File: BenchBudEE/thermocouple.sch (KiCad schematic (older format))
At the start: 0 parts

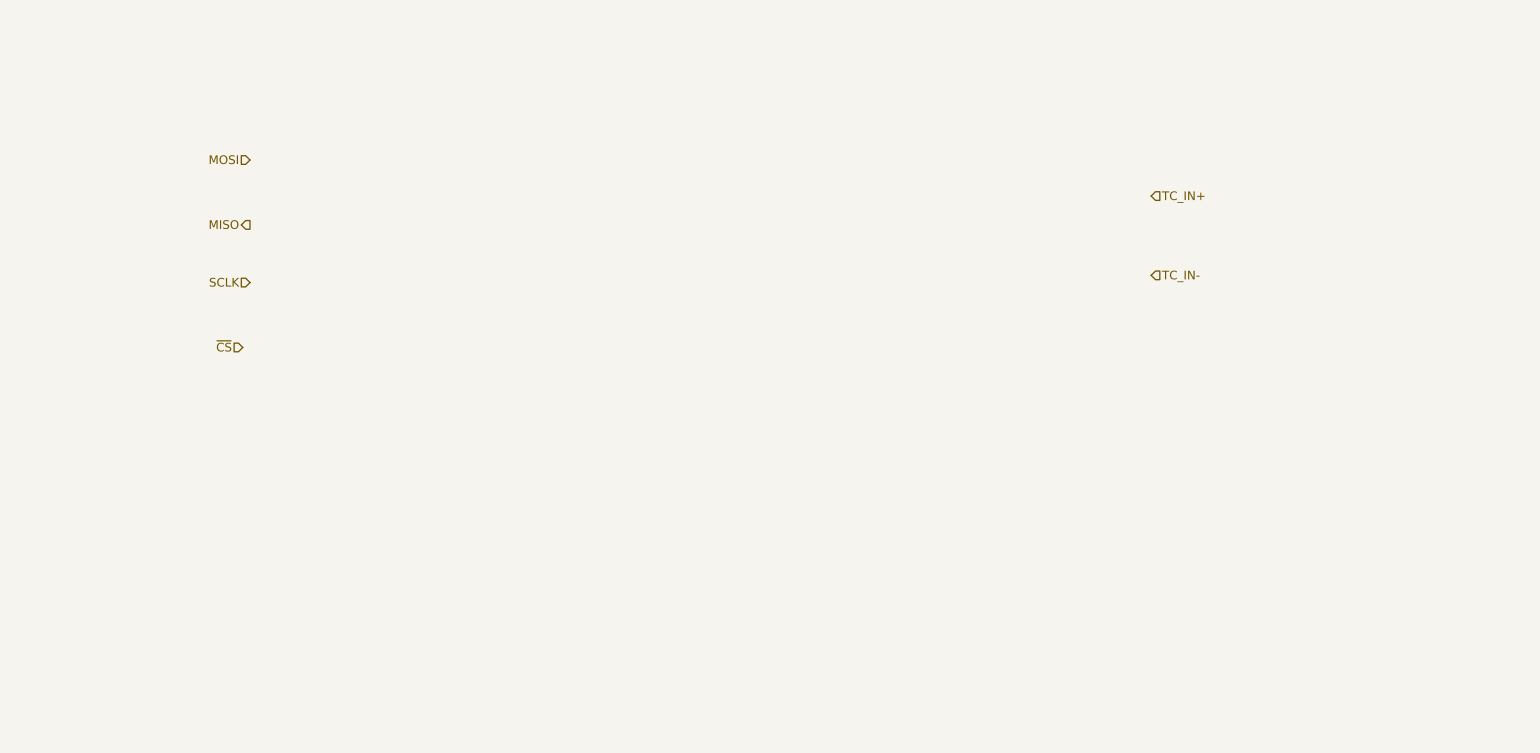
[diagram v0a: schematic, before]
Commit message: blocked TC sheet
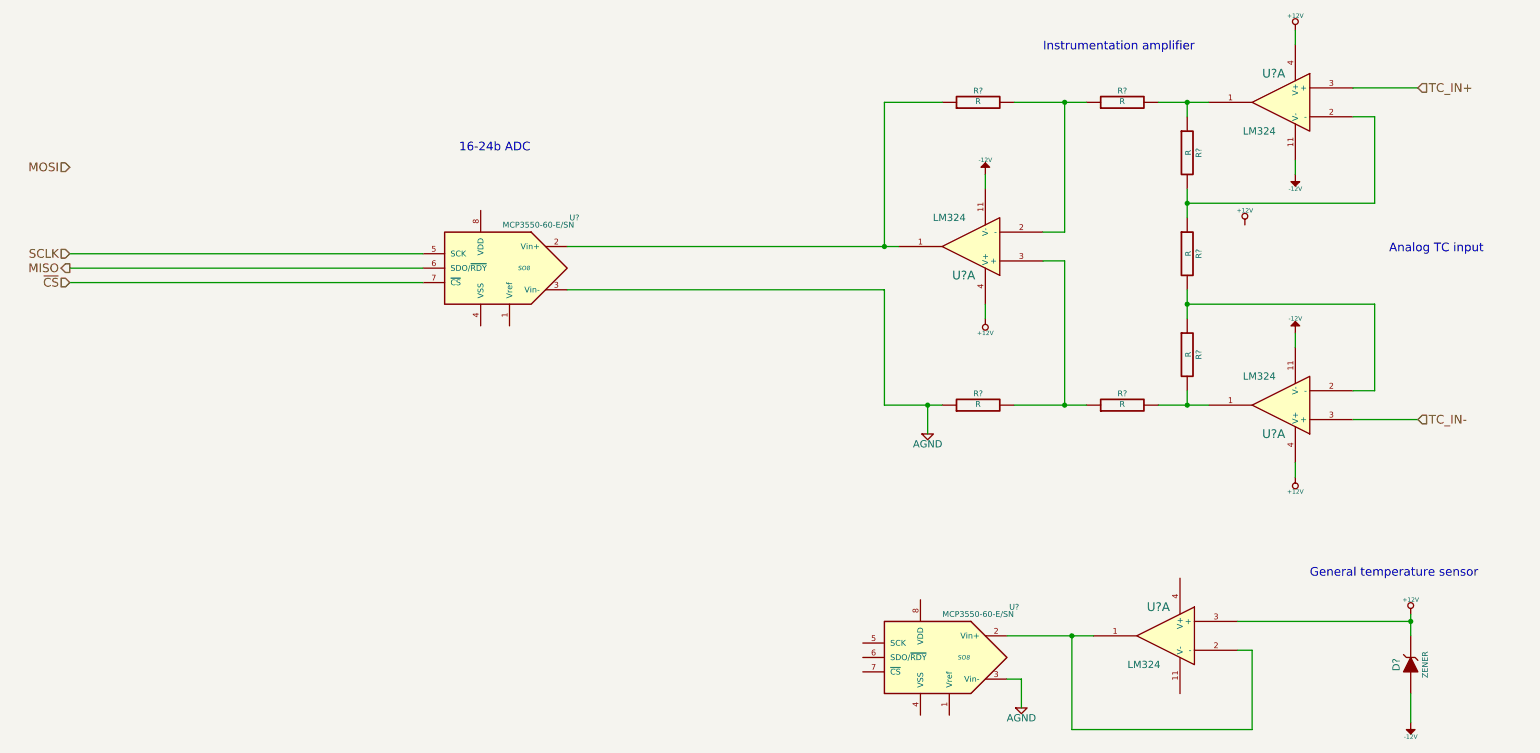
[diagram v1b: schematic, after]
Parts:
- added D?: ZENER, ~, symbol ZENER
- added R? (x7): R, ~, symbol R
- added U? (x4): LM324, symbol LM324
- added U? (x2): MCP3550-60-E/SN, SO8, symbol MCP3550-60-E/SN
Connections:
- net MISO: now also U?.6 (SDO/~RDY~)
- net SCLK: now also U?.5 (SCK)
- net TC_IN+: now also U?.3 (+)
- net TC_IN-: now also U?.3 (+)
- net ~CS: now also U?.7 (~CS~)
- new net: R?.1, R?.2, U?.1
- new net: R?.1, R?.2, U?.2 (-) (x3)
- new net: R?.1, U?.1, U?.2 (Vin+)
- new net: R?.1, R?.2, U?.3 (+)
- new net: R?.2, R?.2, U?.1
- new net: U?.1, U?.2 (-), U?.2 (Vin+)
- new net +12V: D?.2 (K), U?.3 (+), U?.4 (V+), U?.4 (V+), U?.4 (V+)
- new net -12V: D?.1 (A), U?.11 (V-), U?.11 (V-), U?.11 (V-)
- new net AGND: R?.1, U?.3 (Vin-), U?.3 (Vin-)
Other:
- note added: "16-24b ADC"
- note added: "Analog TC input"
- note added: "General temperature sensor"
- note added: "Instrumentation amplifier"
